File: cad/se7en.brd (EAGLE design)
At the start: 64.1 x 34 mm, 59 parts, among them CN1 MICROSD-EJECT, CN3 DO NOT PLACE, CN4 DO NOT PLACE, SW1 SWITCHKMR211, SW2 SWITCHKMR211, U1 ATSAME70, X1 12MHz, X2 32k768

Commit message: charger
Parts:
- removed D1: 1A, jaw:SMD0805D
- added LED3: LED, jaw:SMD0603D
- added Q1: FDC6329S, jaw:SOT-23-6
- added R10: 1M, jaw:SMD0603
- added R11: 1k, jaw:SMD0402
- added R9: 10k, jaw:SMD0603
- added U2: MCP73831/OT, adafruit:SOT23-5L
- C1: value 4u7 -> .1u
- C2, C3: value (none) -> .1u
- L1: value 10u -> 1u
- L2, L3: value (none) -> 1u
- moved U$4 10.3 mm to (66.5, 44.5)
- moved CN2 5.50 mm to (59.5, 49.5)
- moved C20 5.41 mm to (60.5, 56.5), turned to 180 degrees
- moved C10 0.50 mm to (99.5, 55.5)
- moved C6 0.50 mm to (74.5, 46.5)
- moved C7 0.50 mm to (74.5, 44.5)
- moved X2 0.50 mm to (77.5, 45.5)
- moved U$3 0.22 mm to (69.9, 47.8)
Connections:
- removed net N$15: D1.A, F1.2
- new net N$10: LED3.C, U2.1
- new net N$12: LED3.A, R11.1
- new net N$17: R9.1, U2.5
- new net VIN: F1.2, Q1.1, Q1.3, R10.2, R11.2, U2.4
- new net VSYS: Q1.2, Q1.6, VR1.3, VR1.4
- net GND: now also R10.1, R9.2, U2.2
- net VBAT: now also Q1.4, U2.3; no longer D1.C, VR1.3, VR1.4
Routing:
- net VIN: track 0.00 -> 27.5 mm, vias 0 -> 3
- net N$15: track 10.3 -> 0.00 mm
- net VSYS: track 0.00 -> 9.82 mm
- net VBAT: track 41.5 -> 32.7 mm
- net GND: track 89.0 -> 94.3 mm, vias 46 -> 48
- net N$10: track 0.00 -> 2.19 mm
- net N$12: track 0.00 -> 1.70 mm
- net N$17: track 0.00 -> 1.55 mm
- net N$9: track 8.22 -> 7.67 mm
- net N$11: track 6.61 -> 6.06 mm
- net VCC: track 44.8 -> 45.3 mm, vias 17 -> 18
- added copper zone on layer 1, net V1V2
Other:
- board text added: "3V3 GND"
- board text added: "3V3 nRST"
- board text added: "A14 A15"
- board text added: "A16 A13"
- board text added: "A18 A19"
- board text added: "A20 B0"
- board text added: "A21 B3"
- board text added: "A22 D30"
- board text added: "B1 D31"
- board text added: "B2 A17"
- board text added: "CHRG"
- board text added: "CSd GND"
- board text added: "D0 B13"
- board text added: "D26 D25"
- board text added: "D27 A23"
- board text added: "I2C CK DA"
- board text added: "MISO SCK"
- board text added: "MOSI DC"
- board text added: "VBAT GND"
- board text added: "VUSB GND"

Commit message: tweak
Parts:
- added C25: 10u, jaw:SMD0603
- added CN6, CN7: DO NOT PLACE, jaw:HEADER-1X1-SMALL
- C5, C6, C7, R1, R10, R2, R3, R9: device jaw:SMD0603 -> jaw:SMD0402
- CN5: value (none) -> DO NOT PLACE
- L1, L2, L3: value 1u -> FB
- LED1: value LED -> white
- LED3: value LED -> RED
- moved U$1 31.1 mm to (91.2, 58.4)
- moved LOGO1 30.4 mm to (97.9, 55.7)
- moved R10 2.00 mm to (63.5, 54.5)
- moved R2 1.80 mm to (78.5, 65.0), turned to 270 degrees
- moved C23 1.12 mm to (98.5, 65.0)
- moved C6 1.00 mm to (75.5, 46.5), turned to 270 degrees
- moved C7 1.00 mm to (75.5, 44.5), turned to 90 degrees
- moved R1 0.71 mm to (98.5, 66.0)
- moved R3 0.50 mm to (98.5, 67.0)
- moved R5 0.50 mm to (104.5, 60.0)
- turned C5 to 90 degrees
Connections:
- new net PIEZO: CN7.P$1, U1.72
- new net PINA12: U1.48
- net GND: now also C25.2, CN6.P$1
- net VSYS: now also C25.1
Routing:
- net PIEZO: track 0.00 -> 8.36 mm
- net N$16: track 16.4 -> 14.1 mm
- net VSYS: track 9.82 -> 12.0 mm
- net N$7: track 12.9 -> 10.9 mm
- net GND: track 94.3 -> 93.3 mm, vias 48 -> 86
- net NRST: track 82.4 -> 81.8 mm
- added copper zone on layer 1, net GND
- added copper zone on layer 16, net GND
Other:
- board text added: "+"
- board text added: "34mm"
- board text added: "64mm"
- board text added: "ARM"
- board text added: "AT SAM S70"
- board text added: "Cortex"
- board text added: "M7"
- board text added: "MAX: 6V"
- board text added: "Pb"
- board text added: "piezo"
- board text removed: "AMIKETO"
- board text removed: "BATTERY"

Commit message: replace A22 with A12
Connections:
- net PINA12: now also CN5.13
- net PINA13: now also CN5.21; no longer CN5.20
- net PINA14: now also CN5.16; no longer CN5.15
- net PINA15: now also CN5.17; no longer CN5.16
- net PINA16: now also CN5.20; no longer CN5.19
- net PINA22: no longer CN5.21
- net PINA23: now also CN5.19; no longer CN5.18
- net PIND25: now also CN5.15; no longer CN5.14
- net PIND26: now also CN5.14; no longer CN5.13
- net PIND27: now also CN5.18; no longer CN5.17
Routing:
- net PINA12: track 0.00 -> 10.2 mm, vias 0 -> 1
- net PINA22: track 6.27 -> 0.00 mm
- net PINA13: track 13.2 -> 9.42 mm
- net PINA15: track 9.69 -> 6.10 mm
- net PIND25: track 14.9 -> 11.3 mm
- net PINA16: track 5.67 -> 9.20 mm
- net PINA23: track 9.05 -> 5.80 mm
- net PIND26: track 12.2 -> 14.7 mm
- net PIND27: track 6.31 -> 8.85 mm
- net PINA14: track 6.97 -> 9.48 mm
- added copper zone on layer 1, net N$15
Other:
- board text added: "A12 D26"
- board text added: "A13 D30"
- board text added: "A15 D27"
- board text added: "A23 A16"
- board text added: "D25 A14"
- board text added: "VBAT, VUSB: 6V MAX ALL IO PINS: 3.3V MAX"
- board text removed: "A14 A15"
- board text removed: "A16 A13"
- board text removed: "A22 D30"
- board text removed: "D26 D25"
- board text removed: "D27 A23"

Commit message: tweak
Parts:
- moved R11 4.01 mm to (57.2, 58.5), turned to 270 degrees
- moved LED3 1.58 mm to (57.5, 55.5)
- moved R9 0.20 mm to (57.2, 60.5)
- moved U$3 0.20 mm to (70.1, 47.8)
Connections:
- removed net PINA22: U1.26
- net N$10: now also R11.1; no longer LED3.C
- net N$12: now also LED3.C, R11.2; no longer LED3.A, R11.1
- net VIN: now also LED3.A; no longer R11.2
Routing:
- net VCC: track 45.2 -> 58.2 mm, vias 18 -> 17
- net GND: track 93.2 -> 99.3 mm, vias 86 -> 88
- net VBAT: track 32.7 -> 30.5 mm
- net VIN: track 27.1 -> 27.9 mm
- net N$10: track 2.19 -> 1.47 mm
- net ERASE: track 73.8 -> 74.4 mm
- added copper zone on layer 1, net N$18
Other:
- board text added: "LiPO BATTERY"
- board text removed: "MAX: 6V"

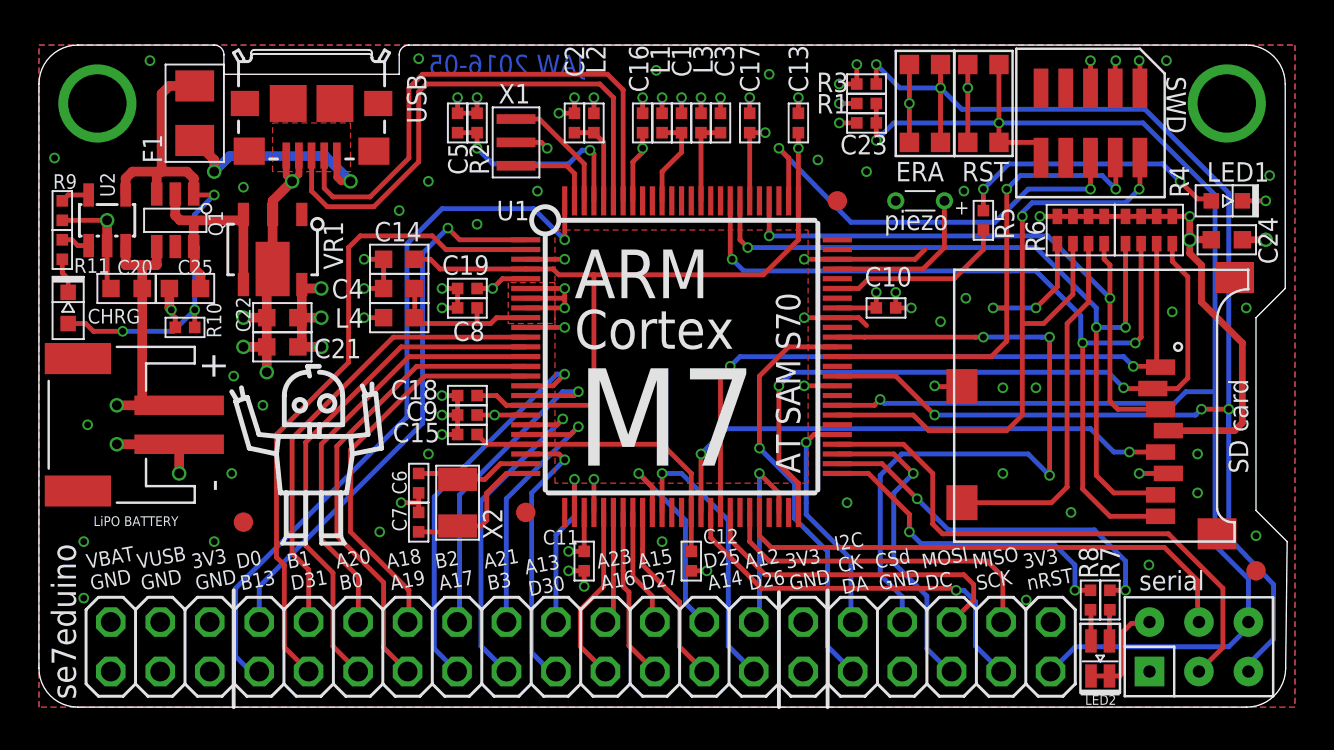
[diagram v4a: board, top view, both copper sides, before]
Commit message: smaller/cheaper regulator
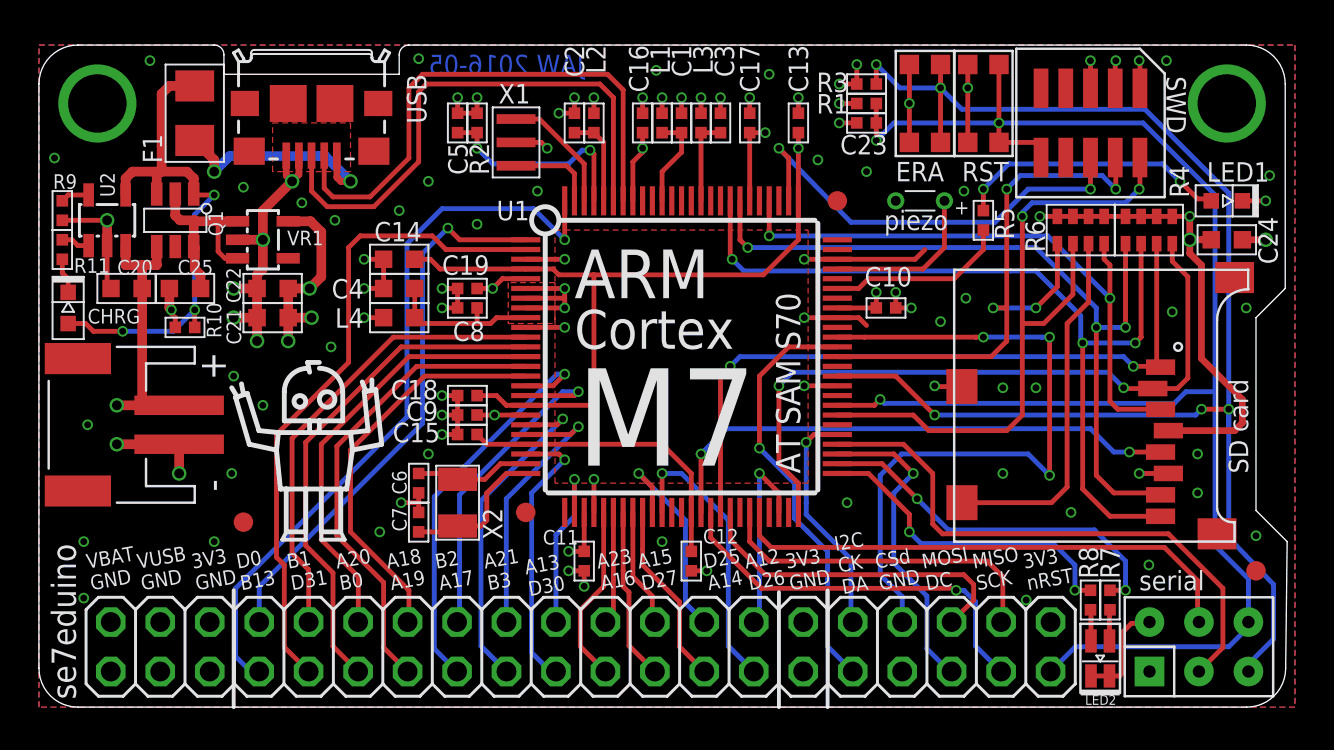
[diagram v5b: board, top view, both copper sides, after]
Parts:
- VR1: value NCP694 -> 3v3, 500mA; device jaw:SOT89-5 -> jaw:SOT-23-5
- moved C21 1.58 mm to (68.0, 55.0)
- moved C22 1.58 mm to (68.0, 56.5)
- moved VR1 0.71 mm to (67.5, 59.0), turned to 0 degrees
- moved U$3 0.20 mm to (70.1, 48.0)
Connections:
- net GND: no longer VR1.2P
- net VSYS: now also VR1.1; no longer VR1.4
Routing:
- net VCC: track 58.2 -> 61.5 mm
- net VSYS: track 12.0 -> 10.9 mm
- net GND: track 99.3 -> 99.2 mm, vias 88 -> 92
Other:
- board text removed: "LiPO BATTERY"
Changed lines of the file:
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@@
 <text x="88.8" y="42.7" size="1.5" layer="22" font="fixed" ratio="15" rot="MR0">VBAT, VUSB:  6V MAX
 ALL IO PINS: 3.3V MAX</text>
-<text x="58.8" y="44.3" size="0.5" layer="21" ratio="15">LiPO BATTERY</text>
 </plain>
 <attributes>
@@
 <attribute name="VALUE" x="62.278" y="58.586" size="1" layer="27" font="vector" ratio="10" rot="R180"/>
 </element>
-<element name="C21" library="jaw" package="SMD0603" value="10u" x="68.5" y="53.5" smashed="yes" rot="R180">
-<attribute name="NAME" x="70.122" y="52.916" size="1" layer="25" font="vector" ratio="10"/>
-<attribute name="VALUE" x="70.278" y="55.586" size="1" layer="27" font="vector" ratio="10" rot="R180"/>
-</element>
-<element name="C22" library="jaw" package="SMD0603" value="1u" x="68.5" y="55" smashed="yes" rot="R180">
-<attribute name="NAME" x="66.116" y="56.078" size="0.75" layer="25" font="vector" ratio="10" rot="R270"/>
-<attribute name="VALUE" x="70.278" y="57.086" size="1" layer="27" font="vector" ratio="10" rot="R180"/>
+<element name="C21" library="jaw" package="SMD0603" value="10u" x="68" y="55" smashed="yes" rot="R180">
+<attribute name="NAME" x="66.384" y="53.622" size="0.75" layer="25" font="vector" ratio="10" rot="R90"/>
+<attribute name="VALUE" x="69.778" y="57.086" size="1" layer="27" font="vector" ratio="10" rot="R180"/>
+</element>
+<element name="C22" library="jaw" package="SMD0603" value="1u" x="68" y="56.5" smashed="yes" rot="R180">
+<attribute name="NAME" x="65.616" y="57.578" size="0.75" layer="25" font="vector" ratio="10" rot="R270"/>
+<attribute name="VALUE" x="69.778" y="58.586" size="1" layer="27" font="vector" ratio="10" rot="R180"/>
 </element>
 <element name="C23" library="jaw" package="SMD0402" value=".1u" x="98.5" y="65" smashed="yes" rot="R180">
@@
 <element name="U$6" library="adafruit" package="FIDUCIAL_1MM" value="FIDUCIAL" x="81" y="45"/>
 <element name="U$1" library="jaw" package="ROBOTMAN-LOGO2" value="ROBOTMAN-LOGO2" x="91.2" y="58.4" rot="MR0"/>
-<element name="U$3" library="jaw" package="ROBOTMAN-LOGO2" value="ROBOTMAN-LOGO2" x="70.1" y="47.8"/>
+<element name="U$3" library="jaw" package="ROBOTMAN-LOGO2" value="ROBOTMAN-LOGO2" x="70.1" y="48"/>
 <element name="LOGO1" library="SparkFun-Aesthetics" package="OSHW-LOGO-M" value="OSHW-LOGOM" x="97.9" y="55.7" rot="MR0"/>
 <element name="U2" library="adafruit" package="SOT23-5L" value="MCP73831/OT" x="59.5" y="60" smashed="yes">
@@
 <attribute name="VALUE" x="57.595" y="56.571" size="1.27" layer="27"/>
 </element>
-<element name="VR1" library="jaw" package="SOT89-5" value="NCP694" x="68" y="58.5" smashed="yes" rot="R180">
-<attribute name="NAME" x="70.6185" y="59.9555" size="1" layer="25" ratio="10" rot="R270"/>
-<attribute name="VALUE" x="64.3095" y="60.9295" size="1" layer="27" ratio="10" rot="R270"/>
+<element name="VR1" library="jaw" package="SOT-23-5" value="3v3, 500mA" x="67.5" y="59" smashed="yes">
+<attribute name="NAME" x="68.7445" y="58.7185" size="0.75" layer="25" ratio="10"/>
+<attribute name="VALUE" x="71.1905" y="56.5705" size="1" layer="27" ratio="10" rot="R90"/>
 </element>
 <element name="R7" library="jaw" package="SMD0402" value="1k" x="111" y="40.5" smashed="yes" rot="R90">
@@
 <via x="62.8" y="55.4" extent="1-16" drill="0.35"/>
 <via x="59.5" y="60" extent="1-16" drill="0.5"/>
-<via x="66.5" y="53.5" extent="1-16" drill="0.5"/>
+<via x="66" y="55" extent="1-16" drill="0.5"/>
 <via x="69" y="62" extent="1-16" drill="0.5"/>
 <wire x1="69.35" y1="63.325" x2="69.35" y2="62.35" width="0.35" layer="1"/>
@@
 <vertex x="56" y="35"/>
 </polygon>
-<contactref element="VR1" pad="2P"/>
 <contactref element="VR1" pad="2"/>
-<via x="67.7" y="52.2" extent="1-16" drill="0.5"/>
-<wire x1="68" y1="57.5" x2="68" y2="60.3" width="0.5" layer="1"/>
-<wire x1="68" y1="60.3" x2="68" y2="61" width="0.5" layer="1"/>
-<wire x1="68" y1="61" x2="69" y2="62" width="0.5" layer="1"/>
-<wire x1="67.7" y1="55" x2="67.7" y2="57.2" width="0.5" layer="1"/>
-<wire x1="67.7" y1="57.2" x2="68" y2="57.5" width="0.5" layer="1"/>
-<wire x1="67.7" y1="53.5" x2="67.7" y2="55" width="0.5" layer="1"/>
-<wire x1="67.7" y1="52.2" x2="67.7" y2="53.5" width="0.5" layer="1"/>
-<wire x1="66.5" y1="53.5" x2="67.7" y2="53.5" width="0.5" layer="1"/>
+<via x="67.2" y="53.8" extent="1-16" drill="0.5"/>
+<wire x1="67.5" y1="60.5" x2="69" y2="62" width="0.5" layer="1"/>
+<wire x1="67.2" y1="55" x2="67.2" y2="56.5" width="0.5" layer="1"/>
+<wire x1="67.2" y1="53.8" x2="67.2" y2="55" width="0.5" layer="1"/>
+<wire x1="66" y1="55" x2="67.2" y2="55" width="0.5" layer="1"/>
 <contactref element="LED2" pad="2"/>
 <contactref element="LED2" pad="3"/>
@@
 <wire x1="57.2" y1="60" x2="59.5" y2="60" width="0.25" layer="1"/>
 <via x="60" y="48.5" extent="1-16" drill="0.5"/>
-<via x="66.5" y="55" extent="1-16" drill="0.5"/>
+<via x="66" y="56.5" extent="1-16" drill="0.5"/>
 <wire x1="63.2" y1="48.5" x2="60" y2="48.5" width="0.5" layer="1"/>
-<wire x1="66.5" y1="55" x2="67.7" y2="55" width="0.5" layer="1"/>
+<wire x1="66" y1="56.5" x2="67.2" y2="56.5" width="0.5" layer="1"/>
 <wire x1="75.5" y1="46" x2="75.5" y2="45.5" width="0.25" layer="1"/>
 <wire x1="75.5" y1="45.5" x2="75.5" y2="45" width="0.25" layer="1"/>
@@
 <via x="102.3" y="54.8" extent="1-16" drill="0.35"/>
 <via x="103.5" y="61.5" extent="1-16" drill="0.35"/>
+<wire x1="67.5" y1="60.5" x2="67.5" y2="59" width="0.5" layer="1"/>
+<wire x1="66.2" y1="59" x2="67.5" y2="59" width="0.5" layer="1"/>
+<wire x1="67.5" y1="59" x2="67.5" y2="57.5" width="0.5" layer="1"/>
+<wire x1="67.5" y1="57.5" x2="67.2" y2="57.2" width="0.5" layer="1"/>
+<wire x1="67.2" y1="57.2" x2="67.2" y2="56.5" width="0.5" layer="1"/>
+<via x="67.5" y="59" extent="1-16" drill="0.5"/>
 <wire x1="81" y1="56.5" x2="81" y2="56" width="0" layer="19" extent="1-1"/>
+<via x="71.2" y="60" extent="1-16" drill="0.35"/>
+<via x="69.5" y="60.9" extent="1-16" drill="0.35"/>
+<via x="71" y="53.5" extent="1-16" drill="0.35"/>
 </signal>
 <signal name="VCC">
@@
 <wire x1="112.54" y1="66.778" x2="112.54" y2="68.16" width="0.25" layer="1"/>
 <wire x1="112.54" y1="68.16" x2="112.5" y2="68.2" width="0.25" layer="1"/>
-<via x="70.5" y="53.5" extent="1-16" drill="0.5"/>
+<via x="68.8" y="53.8" extent="1-16" drill="0.5"/>
 <wire x1="100.7" y1="64" x2="100.7" y2="66" width="0.25" layer="1"/>
 <wire x1="100.7" y1="66" x2="100.7" y2="68" width="0.25" layer="1"/>
@@
 </polygon>
 <contactref element="VR1" pad="5"/>
-<via x="70.5" y="55" extent="1-16" drill="0.5"/>
-<wire x1="69.5" y1="56.7" x2="69.5" y2="56.5" width="0.5" layer="1"/>
-<wire x1="69.5" y1="56.5" x2="69.5" y2="55.2" width="0.5" layer="1"/>
-<wire x1="69.5" y1="55.2" x2="69.3" y2="55" width="0.5" layer="1"/>
-<wire x1="69.5" y1="55.2" x2="69.5" y2="53.7" width="0.5" layer="1"/>
-<wire x1="69.5" y1="53.7" x2="69.3" y2="53.5" width="0.5" layer="1"/>
-<wire x1="70.5" y1="55" x2="69.3" y2="55" width="0.5" layer="1"/>
-<wire x1="70.5" y1="53.5" x2="69.5" y2="53.5" width="0.5" layer="1"/>
-<via x="70.5" y="56.5" extent="1-16" drill="0.5"/>
-<wire x1="70.5" y1="56.5" x2="69.5" y2="56.5" width="0.5" layer="1"/>
+<via x="70" y="55" extent="1-16" drill="0.5"/>
+<via x="69.9" y="56.5" extent="1-16" drill="0.5"/>
 <wire x1="114" y1="49.2" x2="117.4" y2="49.2" width="0.35" layer="1"/>
 <wire x1="117.4" y1="49.2" x2="117.8" y2="49.6" width="0.35" layer="1"/>
-<wire x1="117.8" y1="49.6" x2="117.8" y2="53.7" width="0.35" layer="1"/>
-<wire x1="117.8" y1="53.7" x2="115.7" y2="55.8" width="0.35" layer="1"/>
-<wire x1="115.7" y1="55.8" x2="115.7" y2="57.7" width="0.35" layer="1"/>
+<wire x1="117.8" y1="49.6" x2="117.8" y2="50.8" width="0.35" layer="1"/>
+<wire x1="117.8" y1="50.8" x2="115.7" y2="52.9" width="0.35" layer="1"/>
+<wire x1="115.7" y1="52.9" x2="115.7" y2="57.7" width="0.35" layer="1"/>
 <wire x1="115.7" y1="57.7" x2="115.1" y2="58.3" width="0.35" layer="1"/>
 <wire x1="115.1" y1="58.3" x2="115.1" y2="59" width="0.35" layer="1"/>
+<wire x1="68.8" y1="59.95" x2="69.95" y2="59.95" width="0.5" layer="1"/>
+<wire x1="69.95" y1="59.95" x2="70.5" y2="59.4" width="0.5" layer="1"/>
+<wire x1="70.5" y1="59.4" x2="70.5" y2="57.1" width="0.5" layer="1"/>
+<wire x1="70.5" y1="57.1" x2="69.9" y2="56.5" width="0.5" layer="1"/>
+<wire x1="68.8" y1="56.5" x2="69.9" y2="56.5" width="0.5" layer="1"/>
+<wire x1="68.8" y1="55" x2="70" y2="55" width="0.5" layer="1"/>
+<wire x1="68.8" y1="53.8" x2="68.8" y2="55" width="0.5" layer="1"/>
+<wire x1="68.8" y1="55" x2="68.8" y2="56.5" width="0.5" layer="1"/>
 </signal>
 <signal name="V1V2">
@@
 </signal>
 <signal name="VSYS">
-<contactref element="VR1" pad="4"/>
+<contactref element="VR1" pad="1"/>
 <contactref element="VR1" pad="3"/>
 <contactref element="Q1" pad="2"/>
 <contactref element="Q1" pad="6"/>
-<wire x1="66.5" y1="60.3" x2="66.5" y2="60" width="0.5" layer="1"/>
-<wire x1="66.5" y1="60" x2="66.5" y2="56.7" width="0.5" layer="1"/>
 <wire x1="63" y1="61.35" x2="63" y2="60.25" width="0.5" layer="1"/>
 <wire x1="63" y1="60.25" x2="63.25" y2="60" width="0.5" layer="1"/>
 <wire x1="63.25" y1="60" x2="64" y2="60" width="0.5" layer="1"/>
-<wire x1="64" y1="60" x2="66.5" y2="60" width="0.5" layer="1"/>
 <wire x1="63.95" y1="58.65" x2="63.95" y2="58.95" width="0.5" layer="1"/>
 <wire x1="63.95" y1="58.95" x2="63.95" y2="59.95" width="0.5" layer="1"/>
@@
 <wire x1="64" y1="57.5" x2="64" y2="58.6" width="0.5" layer="1"/>
 <wire x1="64" y1="58.6" x2="63.95" y2="58.65" width="0.5" layer="1"/>
+<wire x1="66.2" y1="59.95" x2="65.4" y2="59.95" width="0.5" layer="1"/>
+<wire x1="65.4" y1="59.95" x2="64.05" y2="59.95" width="0.5" layer="1"/>
+<wire x1="64.05" y1="59.95" x2="64" y2="60" width="0.5" layer="1"/>
+<wire x1="66.2" y1="58.05" x2="65.55" y2="58.05" width="0.25" layer="1"/>
+<wire x1="65.55" y1="58.05" x2="65.2" y2="58.4" width="0.25" layer="1"/>
+<wire x1="65.2" y1="58.4" x2="65.2" y2="59.85" width="0.25" layer="1"/>
+<wire x1="65.2" y1="59.85" x2="65.4" y2="59.95" width="0.25" layer="1"/>
 </signal>
 <signal name="N$17">

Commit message: tweak
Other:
- board size 64.1 x 34 mm -> 64 x 34 mm
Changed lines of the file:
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@@
 <grid distance="0.1" unitdist="mm" unit="mm" style="lines" multiple="5" display="yes" altdistance="0.025" altunitdist="inch" altunit="inch"/>
 <layers>
-<layer number="1" name="Top" color="4" fill="1" visible="yes" active="yes"/>
+<layer number="1" name="Top" color="4" fill="1" visible="no" active="yes"/>
 <layer number="2" name="Route2" color="6" fill="1" visible="no" active="yes"/>
 <layer number="3" name="Route3" color="4" fill="3" visible="no" active="no"/>
 <layer number="14" name="Route14" color="1" fill="6" visible="no" active="no"/>
 <layer number="15" name="Route15" color="13" fill="1" visible="no" active="yes"/>
-<layer number="16" name="Bottom" color="1" fill="1" visible="yes" active="yes"/>
+<layer number="16" name="Bottom" color="1" fill="1" visible="no" active="yes"/>
 <layer number="17" name="Pads" color="2" fill="1" visible="yes" active="yes"/>
 <layer number="18" name="Vias" color="2" fill="1" visible="yes" active="yes"/>
@@
 <wire x1="58" y1="35" x2="118.023390625" y2="35" width="0" layer="20"/>
 <wire x1="118.023390625" y1="35" x2="120.023253125" y2="36.976515625" width="0" layer="20" curve="89.327207"/>
-<wire x1="120.023253125" y1="36.976515625" x2="120.1" y2="43.5" width="0" layer="20"/>
-<wire x1="120.1" y1="43.5" x2="118.5" y2="45.1" width="0" layer="20"/>
-<wire x1="118.5" y1="45.1" x2="118.5" y2="55" width="0" layer="20"/>
+<wire x1="120.023253125" y1="36.976515625" x2="120" y2="43.5" width="0" layer="20"/>
+<wire x1="120" y1="43.5" x2="118.5" y2="45" width="0" layer="20"/>
+<wire x1="118.5" y1="45" x2="118.5" y2="55" width="0" layer="20"/>
 <wire x1="118.5" y1="55" x2="120" y2="56.5" width="0" layer="20"/>
 <wire x1="120" y1="56.5" x2="120" y2="67" width="0" layer="20"/>
@@
 <wire x1="67.2" y1="57.2" x2="67.2" y2="56.5" width="0.5" layer="1"/>
 <via x="67.5" y="59" extent="1-16" drill="0.5"/>
-<wire x1="81" y1="56.5" x2="81" y2="56" width="0" layer="19" extent="1-1"/>
 <via x="71.2" y="60" extent="1-16" drill="0.35"/>
 <via x="69.5" y="60.9" extent="1-16" drill="0.35"/>
 <via x="71" y="53.5" extent="1-16" drill="0.35"/>
+<wire x1="81" y1="56.5" x2="81" y2="56" width="0" layer="19" extent="1-1"/>
 </signal>
 <signal name="VCC">
